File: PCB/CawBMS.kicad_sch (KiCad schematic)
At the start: 37 parts, among them CN1 SWD, CN2 I2C, CN3 SPI, CN4 USART, CN5 SWD, SW1 B3U-1000P, SW2 B3U-1000P, U1 STM32F103CBTx, U2 TCAN1044DRBRQ1, U5 CAN, X1 Crystal_16MHz_15pF_3P

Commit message: Signed-off-by: jasperThinkpad <2567434944@qq.com>
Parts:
- removed U1: STM32F103CBTx, Package_QFP:LQFP-48_7x7mm_P0.5mm, symbol MCU_ST_STM32F1:STM32F103CBTx
- removed U2: TCAN1044DRBRQ1, Rick_CAN:TCAN1044DRBRQ1_DFN-8_L3.0-W3.0-P0.65-TL-EP2.4, symbol Rick_CAN:TCAN1044DRBRQ1
- added U1: SIT1051AT/3, Rick_CAN:ISO1044BDR_SOP-8, symbol bms:CAN
- added U2: STM32F103C_8-B_Tx, Package_QFP:LQFP-48_7x7mm_P0.5mm, symbol bms:STM32F103CBTx
- CN6: renamed from CN1; value SWD -> POWER
- renumbered C5 to C1, C7 to C2, C8 to C3, C1 to C4, C2 to C5, C3 to C6, C4 to C7, C6 to C8, U5 to CN1, CN5 to CN2, CN2 to CN3, CN3 to CN4, CN4 to CN5, R6 to R1, R4 to R3, R5 to R4, R1 to R5, R8 to R6, R3 to R7, R7 to R8
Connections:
- net +3.3V: now also U1.5 (VIO), U2.1 (VBAT), U2.24 (VDD), U2.36 (VDD), U2.48 (VDD)
- net +3.3VA: now also U2.9 (VDDA)
- net +5V: now also U1.3 (VCC)
- net ALERT: now also U2.2 (PC13)
- net CAN_N: now also U1.6 (CANL)
- net CAN_P: now also U1.7 (CANH)
- net CAN_RX: now also U1.4 (RXD), U2.32 (PA11)
- net CAN_TX: now also U1.1 (TXD), U2.33 (PA12)
- net GND: now also U1.2 (GND), U2.23 (VSS), U2.35 (VSS), U2.47 (VSS)
- net HSE_IN: now also U2.5 (PD0)
- net HSE_OUT: now also U2.6 (PD1)
- net I2C1_SCL: now also U2.45 (PB8)
- net I2C1_SDA: now also U2.46 (PB9)
- net I2C2_SCL: now also U2.21 (PB10)
- net I2C2_SDA: now also U2.22 (PB11)
- net KEY_A: now also U2.30 (PA9)
- net LED_A: now also U2.3 (PC14)
- net LED_B: now also U2.4 (PC15)
- net RESET: now also U2.7 (NRST)
- net SPI1_MISO: now also U2.40 (PB4)
- net SPI1_MOSI: now also U2.41 (PB5)
- net SPI1_NSS: now also U2.38 (PA15)
- net SPI1_SCK: now also U2.39 (PB3)
- net SWCLK: now also U2.37 (PA14)
- net SWDIO: now also U2.34 (PA13)
- net USART1_RX: now also U2.43 (PB7)
- net USART1_TX: now also U2.42 (PB6)
- net at R5.2: now also U2.20 (PB2)
- net at R7.1: now also U2.8 (VSSA)
- net at R2.2: now also U2.44 (BOOT0)
- new net CAN_S: U1.8 (S), U2.31 (PA10)
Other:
- moved on the sheet: C1, C2, C3, C4, C5, C6, C7, C8, CN1, CN2, CN3, CN4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

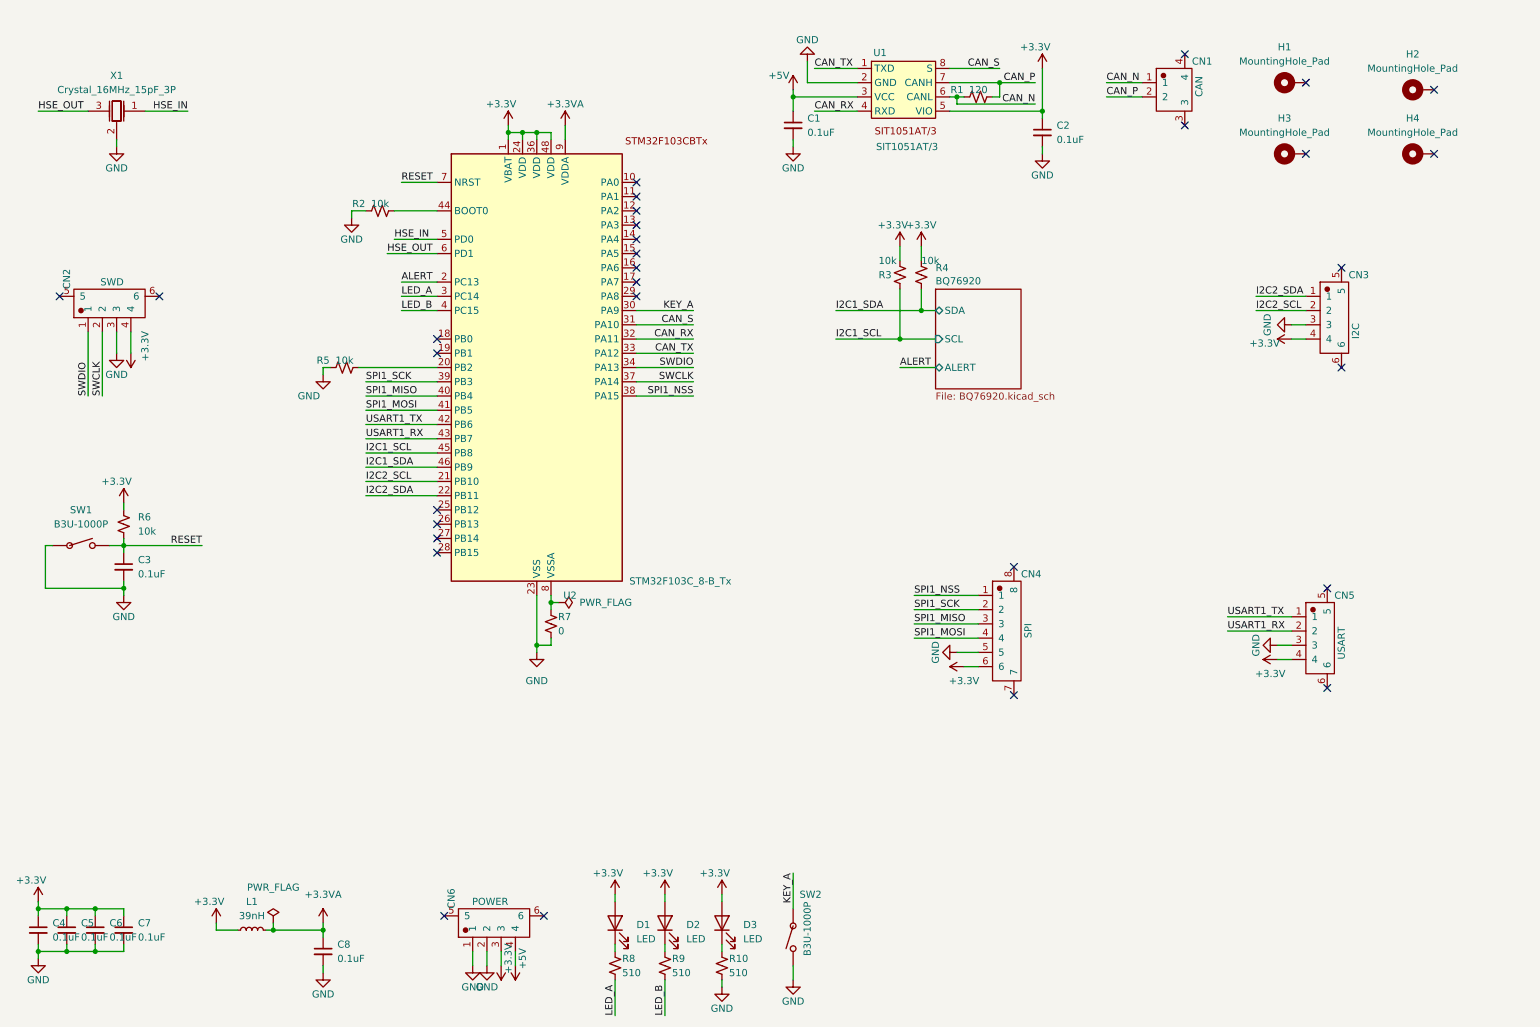
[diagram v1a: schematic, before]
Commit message: 3.5 布局完成
Signed-off-by: jasper <2567434944@qq.com>
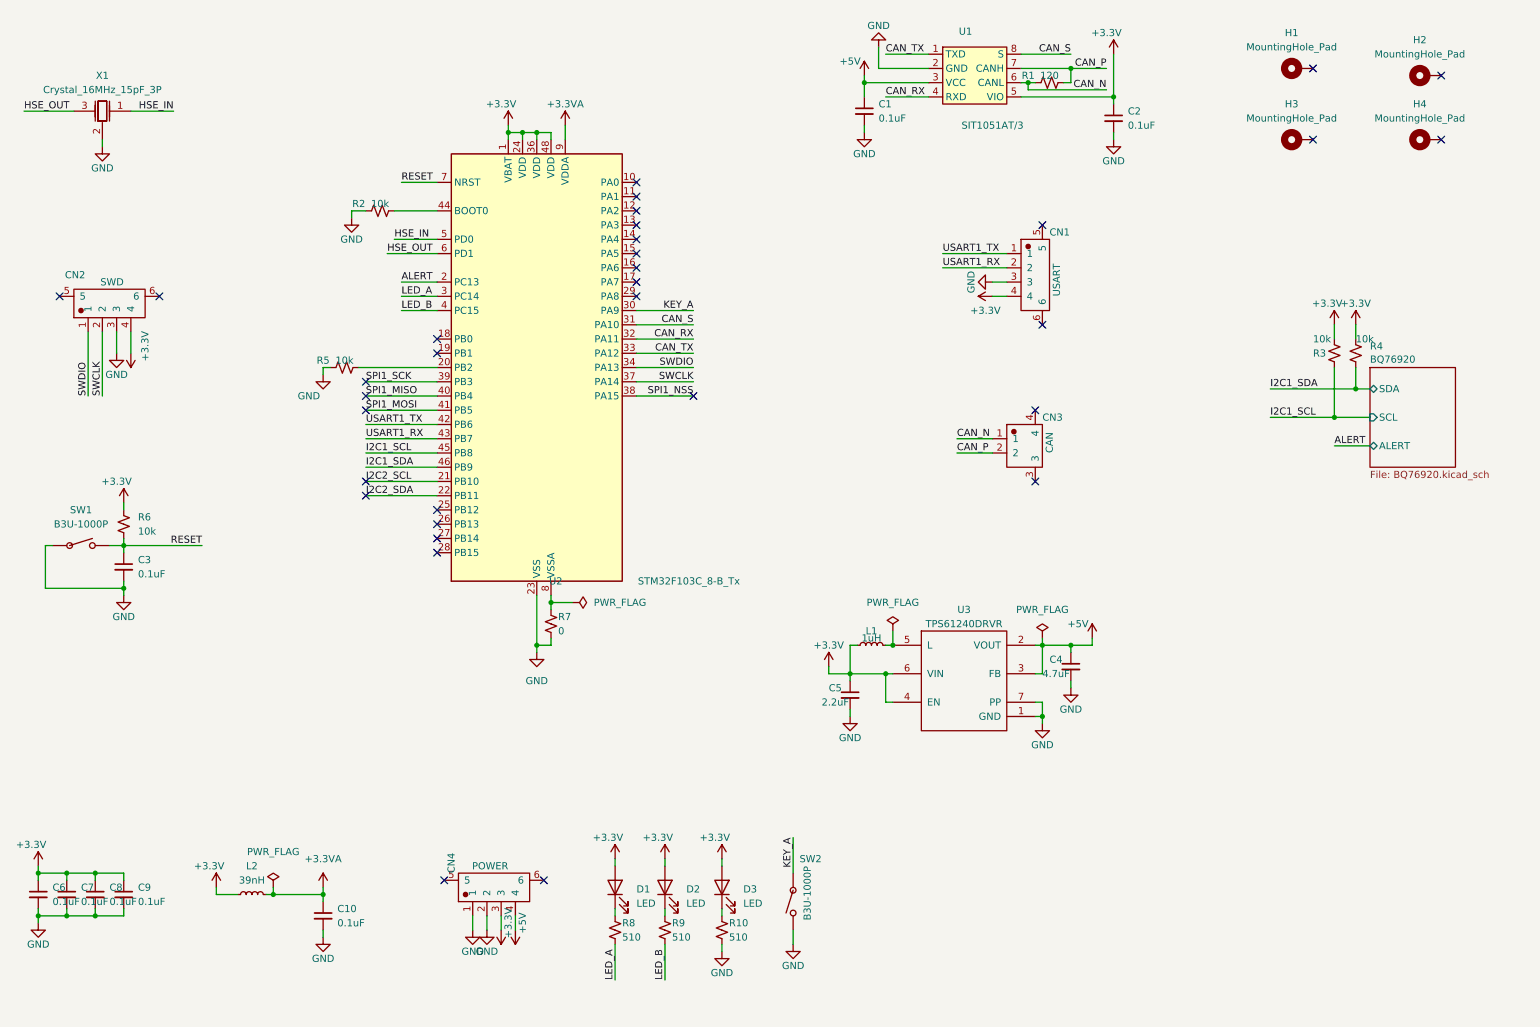
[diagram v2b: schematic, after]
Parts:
- removed CN3: I2C, Rick_Connector:CONN-SMD_4P-P1.00_WAFER-SH1.0-4PWB, symbol Rick_Connector:WAFER-SH1.0-4PWB
- removed CN4: SPI, Rick_Connector:CONN-SMD_6P-P1.00_XUNPU_WAFER-SH1.0-6PWB, symbol Rick_Connector:WAFER-SH1.0-6PWB
- added C4: 4.7uF, Capacitor_SMD:C_0402_1005Metric_Pad0.74x0.62mm_HandSolder, symbol Device:C_Small
- added C5: 2.2uF, Capacitor_SMD:C_0402_1005Metric_Pad0.74x0.62mm_HandSolder, symbol Device:C_Small
- added L1: 1uH, Inductor_SMD:L_1210_3225Metric_Pad1.42x2.65mm_HandSolder, symbol Device:L_Small
- added U3: TPS61240DRVR, Rick_DC-DC:TPS61240DRVR_WSON-6_L2.0-W2.0-P0.65-TL-EP, symbol Rick_DC-DC:TPS61240DRVR
- U1: symbol bms:CAN -> bms:CAN
- U2: symbol bms:STM32F103CBTx -> MCU_ST_STM32F1:STM32F103C_8-B_Tx
- renumbered C8 to C10, C4 to C6, C5 to C7, C6 to C8, C7 to C9, CN5 to CN1, CN1 to CN3, CN6 to CN4, L1 to L2
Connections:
- net +3.3V: now also C5.1, L1.1, U3.4 (EN), U3.6 (VIN)
- net +5V: now also C4.1, U3.2 (VOUT), U3.3 (FB)
- net GND: now also C4.2, C5.2, U3.1 (GND), U3.7 (PP)
- new net: L1.2, U3.5 (L)
- no-connect marks 31 -> 33
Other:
- moved on the sheet: C1, C10, C2, C6, C7, C8, C9, CN1, CN3, CN4, D1, D2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
